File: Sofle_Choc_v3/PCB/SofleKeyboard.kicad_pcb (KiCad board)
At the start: 2 copper layers, 143.5 x 111.4 mm, 93 parts, among them J1 4PIN, J2 OLED, J3 nice!view, J4 B+, J5 B-, SW1 SW_PUSH_LED, SW10 SW_PUSH_LED, SW11 SW_PUSH_LED, SW12 SW_PUSH_LED, SW13 SW_PUSH_LED, SW14 SW_PUSH_LED, SW15 SW_PUSH_LED, SW16 SW_PUSH_LED, SW17 SW_PUSH_LED, SW18 SW_PUSH_LED, SW19 SW_PUSH_LED, SW2 SW_PUSH_LED, SW20 SW_PUSH_LED, SW21 SW_PUSH_LED, SW22 SW_PUSH_LED, SW23 SW_PUSH_LED, SW24 SW_PUSH_LED, SW25 Rotary_Encoder_Switch, SW26 SW_PUSH_LED, SW27 SW_PUSH_LED, SW28 SW_PUSH_LED, SW29 SW_PUSH_LED, SW3 SW_PUSH_LED, SW30 SW_PUSH_LED, SW31 PWR Top, SW32 PWR Bottom, SW4 SW_PUSH_LED, SW5 SW_PUSH_LED, SW6 SW_PUSH_LED, SW7 SW_PUSH_LED, SW8 SW_PUSH_LED, SW9 SW_PUSH_LED, U1 ProMicro

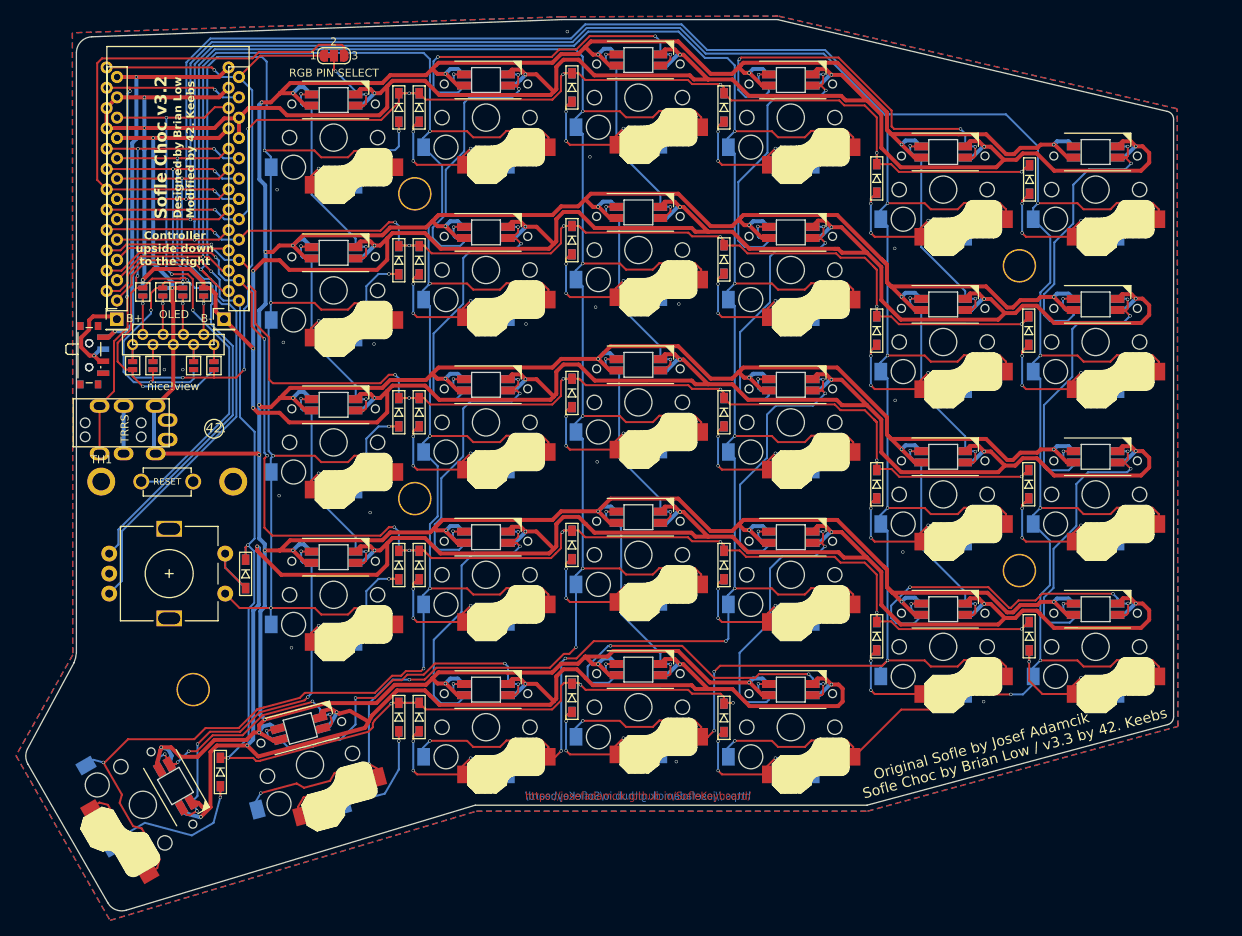
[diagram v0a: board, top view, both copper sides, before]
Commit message: Sofle Choc: add support for extra switch instead of encoder
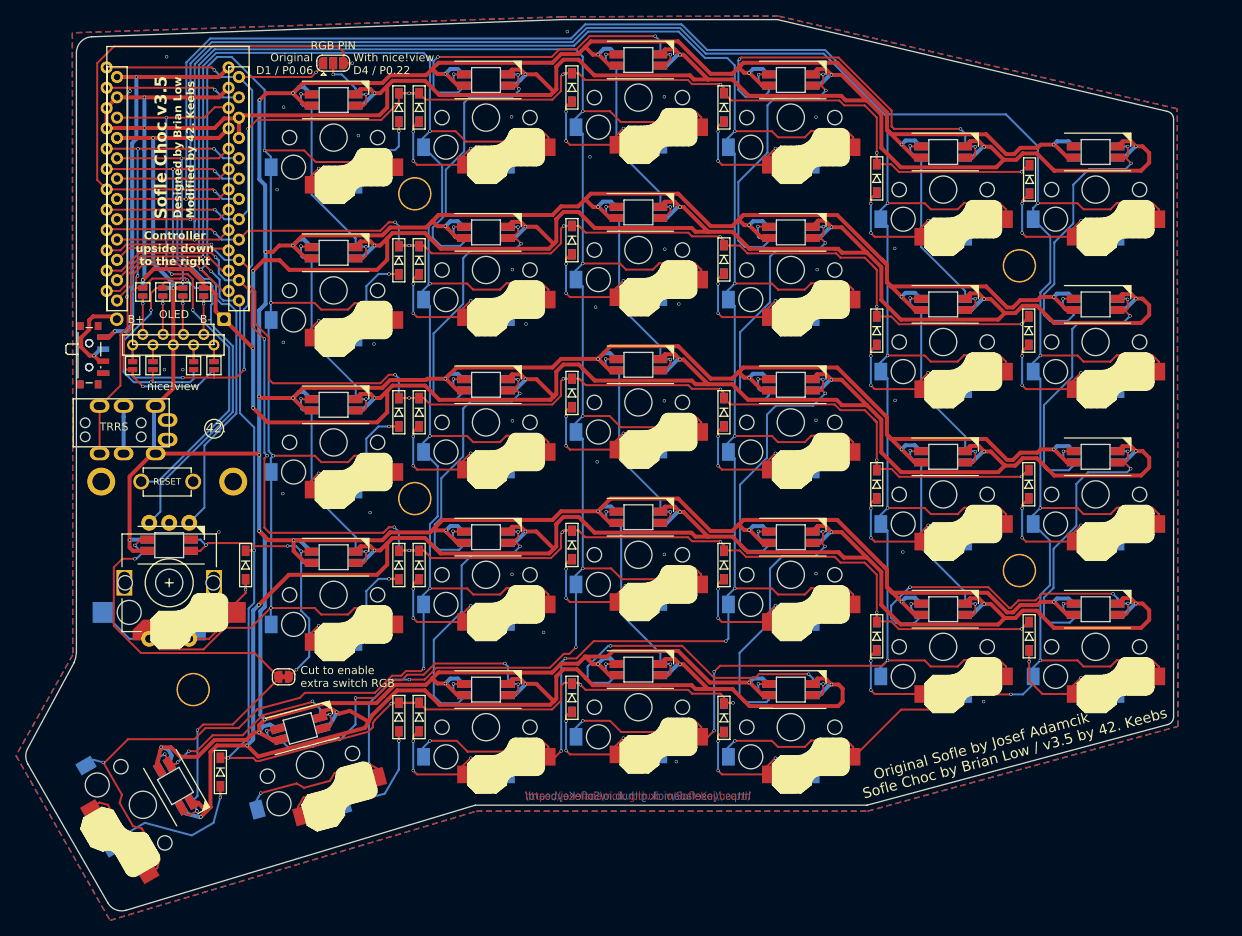
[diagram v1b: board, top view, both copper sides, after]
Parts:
- added JP18: RGB PIN, Jumper:SolderJumper-3_P1.3mm_Open_RoundedPad1.0x1.5mm, F.Cu at (120.5, 40.7)
- added JP19: RGB PIN, Jumper:SolderJumper-3_P1.3mm_Open_RoundedPad1.0x1.5mm, B.Cu at (120.5, 40.7)
- added SW25: SW_PUSH_LED, SofleChoc:Choc_Hotswap_SK6812MiniE_alt_pads_w_cutouts, F.Cu at (100.0, 105.7)
- D1, D10, D11, D12, D13, D14, D15, D16, D17, D18, D19, D2, D20, D21, D22, D23, D24, D25, D26, D27, D28, D29, D3, D30, D4, D5, D6, D7, D8, D9: footprint SofleChoc:crkbd-diode -> SofleChoc:SOD-123_with_cutout
- J1: footprint SofleChoc:MJ-4PP-9 -> SofleChoc:PJ-320A_double_sided_with_cutouts
- J2: footprint SofleChoc:OLED_4Pin -> SofleChoc:OLED_4Pin_with_cutouts
- J3: footprint SofleChoc:niceview_5Pin -> SofleChoc:niceview_5Pin_with_cutouts
- J4: footprint Connector_PinHeader_2.54mm:PinHeader_1x01_P2.54mm_Vertical -> SofleChoc:PinHeader_1x01_P2.54mm_Vertical_B+
- J5: footprint Connector_PinHeader_2.54mm:PinHeader_1x01_P2.54mm_Vertical -> SofleChoc:PinHeader_1x01_P2.54mm_Vertical_B-
- JP17: value Jumper_3_Bridged12 -> SW25 RGB; footprint Jumper:SolderJumper-3_P1.3mm_Bridged12_RoundedPad1.0x1.5mm_NumberLabels -> Jumper:SolderJumper-2_P1.3mm_Bridged_RoundedPad1.0x1.5mm
- RSW1: footprint SofleChoc:TACT_SWITCH_TVBP06 -> SofleChoc:TACT_SWITCH_TVBP06_with_cutouts
- SW1, SW10, SW11, SW12, SW13, SW14, SW15, SW16, SW17, SW18, SW19, SW2, SW20, SW21, SW22, SW23, SW24, SW26, SW27, SW28, SW29, SW3, SW30, SW4, SW5, SW6, SW7, SW8, SW9: footprint SofleChoc:Choc_Hotswap_SK6812MiniE -> SofleChoc:Choc_Hotswap_SK6812MiniE_with_cutouts
- U1: footprint SofleChoc:ProMicro -> SofleChoc:ProMicro_with_cutouts
- moved JP17 77.9 mm to (114.3, 117.4)
- moved SWE25 1.15 mm to (100.0, 105.7), turned to -90 degrees
- moved D25 1.10 mm to (109.5, 103.4)
- renumbered SW25 to SWE25
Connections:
- JP17 pad 1: CS/LED -> Net-(JP17-A)
- JP17 pad 2: LED -> Net-(JP17-B)
- SW19 pad 2: Net-(SW19B-DOUT) -> Net-(JP17-B)
- SW26 pad 4: Net-(SW19B-DOUT) -> Net-(JP17-A)
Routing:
- net Net-(JP17-A): track 0.00 -> 65.6 mm, vias 0 -> 4
- net Net-(SW19B-DOUT): track 48.3 -> 0.00 mm, vias 4 -> 0
- net Net-(JP17-B): track 0.00 -> 36.6 mm, vias 0 -> 4
- net SW25A: track 199.8 -> 217.9 mm
- net ENCB: track 76.8 -> 65.3 mm
- net VCC: track 884.4 -> 895.5 mm, vias 37 -> 38
- net GND: track 1034.9 -> 1026.4 mm, vias 56 -> 72
- net ENCA: track 73.8 -> 66.3 mm
- net SW25B: track 10.7 -> 13.5 mm, vias 0 -> 1
- net LED2: track 66.3 -> 68.9 mm, vias 1 -> 2
- net row4: track 163.7 -> 161.3 mm
- net col3: track 286.9 -> 288.4 mm
- net CS/LED: track 82.6 -> 83.8 mm, vias 3 -> 4
- net LED: track 9.93 -> 11.0 mm
- net SDA: track 68.9 -> 68.2 mm
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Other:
- board text added: "Cut to enable extra switch RGB"
- board text added: "Original D1 / P0.06"
- board text added: "Sofle Choc by Brian Low / v3.5 by 42. Keebs"
- board text added: "Sofle Choc v3.5"
- board text added: "With nice!view D4 / P0.22"
- board text removed: "2"
- board text removed: "RGB PIN SELECT"
- board text removed: "Sofle Choc by Brian Low / v3.3 by 42. Keebs"
- board text removed: "Sofle Choc v3.2"
